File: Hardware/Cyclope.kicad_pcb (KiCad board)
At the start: 2 copper layers, 100 x 84 mm, 81 parts, among them J1 M20-9762042, J2 Motor_2, J3 Motor_1, J4 Front, J5 Front, J8 FTDI, M1 FS5113R, M2 FS5113R, Q1 DMG3414U, Q2 DMG2301L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

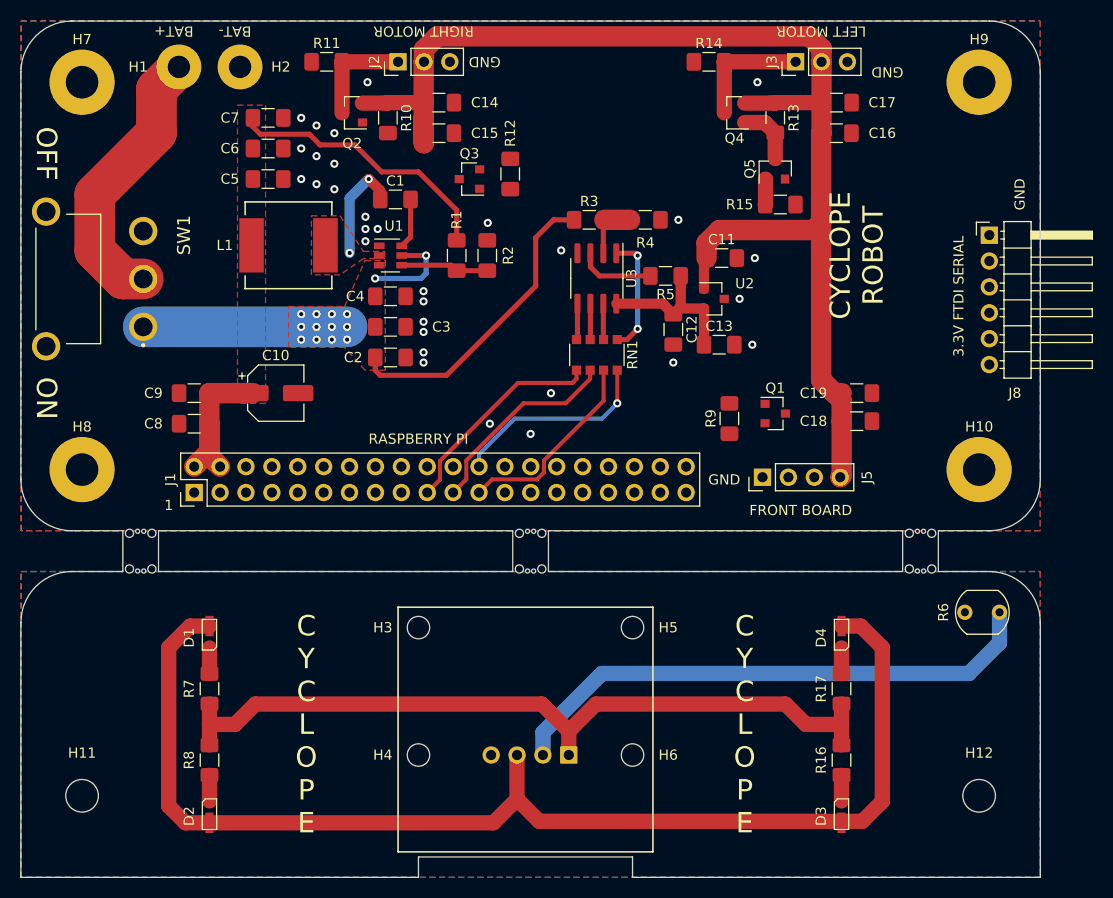
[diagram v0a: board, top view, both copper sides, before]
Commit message: [Hardware] Added larger tracks and a return path for motherboard PCB +5V.
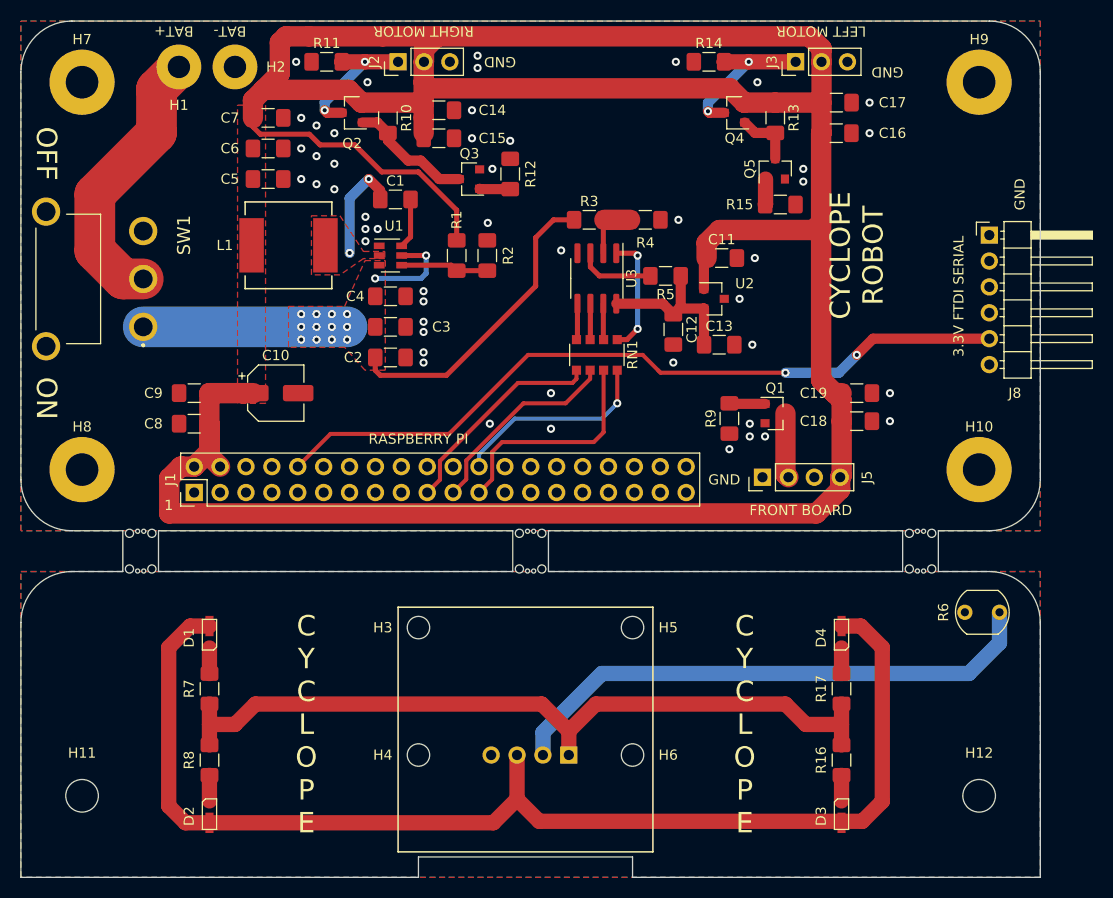
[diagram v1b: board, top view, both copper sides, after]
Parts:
- moved C14 0.75 mm to (98.5, 68.8)
- moved C15 0.50 mm to (98.5, 71.5)
- moved H2 0.50 mm to (78.5, 64.5)
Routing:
- net +5V: track 171.7 -> 317.3 mm
- net /Raspberry_Pi/UART_RX: track 0.00 -> 74.5 mm, vias 0 -> 2
- net Net-(Q2-Pad1): track 0.00 -> 12.2 mm
- net Net-(J5-Pad2): track 0.00 -> 6.37 mm
- net FRONT_BOARD_LEDS: track 0.00 -> 3.52 mm
- net Net-(J2-Pad1): track 10.5 -> 13.7 mm, vias 0 -> 2
- net Net-(J3-Pad1): track 12.0 -> 15.2 mm, vias 0 -> 2
- net Net-(J1-Pad33): track 0.00 -> 3.02 mm
- net ADC_SPI_SCK: track 19.6 -> 22.3 mm
- net GND: vias 31 -> 49

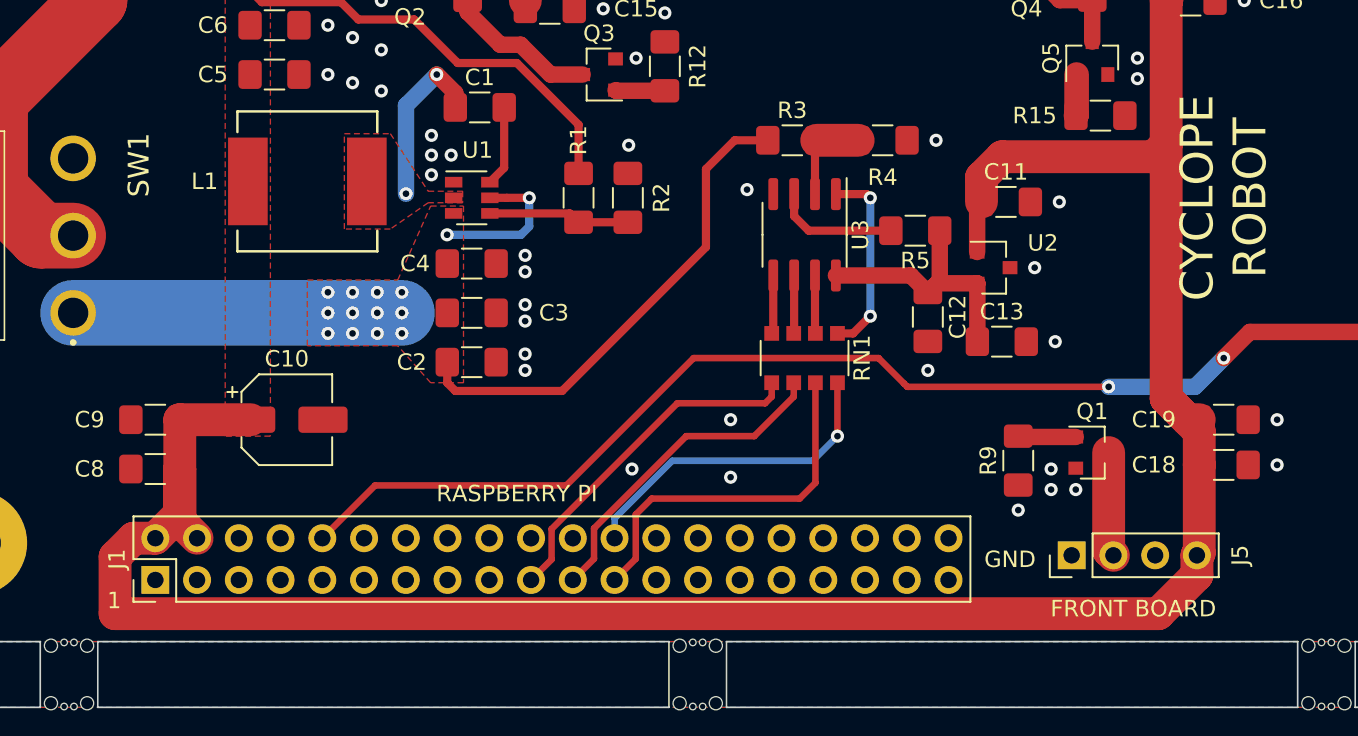
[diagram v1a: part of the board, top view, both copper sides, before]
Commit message: [Hardware] Changed some motherboard connectors connection type with ground planes to decrease impedance.
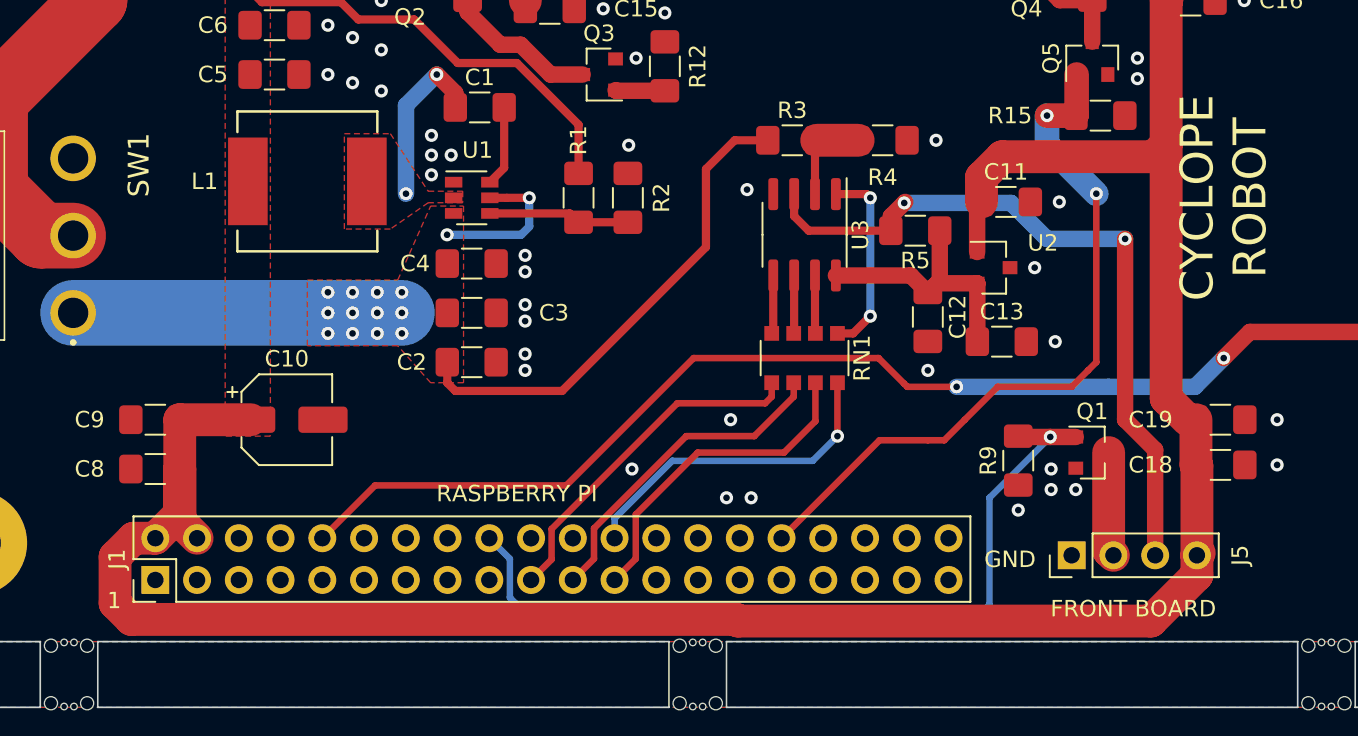
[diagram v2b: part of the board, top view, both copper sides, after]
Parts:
- moved C18 0.20 mm to (139.3, 99.2)
- moved C19 0.20 mm to (139.3, 96.5)
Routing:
- net FRONT_BOARD_LEDS: track 3.52 -> 49.2 mm, vias 0 -> 1
- net Net-(J1-Pad32): track 2.52 -> 44.1 mm, vias 0 -> 2
- net FRONT_BOARD_LDR: track 7.59 -> 44.1 mm, vias 0 -> 2
- net +5V: track 317.3 -> 314.6 mm
- net ADC_SPI_SCK: track 22.3 -> 20.1 mm
- net GND: vias 49 -> 50

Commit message: [Hardware] Improved component names placement on motherboard PCB.
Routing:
- net /Raspberry_Pi/UART_TX: track 0.00 -> 87.5 mm
- net Net-(J1-Pad33): track 3.02 -> 40.1 mm, vias 0 -> 1
- net GND: vias 50 -> 52
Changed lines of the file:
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@@
     (thickness 1.6)
     (drawings 66)
-    (tracks 355)
+    (tracks 376)
     (zones 0)
     (modules 81)
@@
   )
   (setup
-    (last_trace_width 2)
+    (last_trace_width 0.4)
     (user_trace_width 0.4)
     (user_trace_width 0.5)
@@
     (tags "capacitor handsolder")
     (attr smd)
-    (fp_text reference C12 (at 0 -1.82 90) (layer F.SilkS)
+    (fp_text reference C12 (at 0 2 90) (layer F.SilkS)
       (effects (font (size 1 1) (thickness 0.15)))
     )
@@
     (tags "mounting hole 2.2mm m2")
     (attr virtual)
-    (fp_text reference H1 (at 0 3.75) (layer F.SilkS)
+    (fp_text reference H1 (at -3.75 0) (layer F.SilkS)
       (effects (font (size 1 1) (thickness 0.15)))
     )
@@
     (tags "capacitor handsolder")
     (attr smd)
-    (fp_text reference C4 (at 3.45 0) (layer F.SilkS)
+    (fp_text reference C4 (at -4.75 0) (layer F.SilkS)
       (effects (font (size 1 1) (thickness 0.15)))
     )
@@
     (tags "capacitor handsolder")
     (attr smd)
-    (fp_text reference C3 (at -5 0) (layer F.SilkS)
+    (fp_text reference C3 (at -4.75 0) (layer F.SilkS)
       (effects (font (size 1 1) (thickness 0.15)))
     )
@@
     (tags "capacitor handsolder")
     (attr smd)
-    (fp_text reference C2 (at 3.65 0) (layer F.SilkS)
+    (fp_text reference C2 (at -4.75 0) (layer F.SilkS)
       (effects (font (size 1 1) (thickness 0.15)))
     )
@@
     (effects (font (size 1 1) (thickness 0.15)))
   )
-  (gr_text GND (at 142.5 65 180) (layer F.SilkS)
+  (gr_text GND (at 143.5 64 180) (layer F.SilkS)
     (effects (font (size 1 1) (thickness 0.15)))
   )
@@
   (via (at 101.75 68.75) (size 0.8) (drill 0.4) (layers F.Cu B.Cu) (net 3))
   (via (at 84.5 64) (size 0.8) (drill 0.4) (layers F.Cu B.Cu) (net 3))
-  (via (at 102.3 63.4) (size 0.8) (drill 0.4) (layers F.Cu B.Cu) (net 3))
-  (via (at 102.3 64.6) (size 0.8) (drill 0.4) (layers F.Cu B.Cu) (net 3))
+  (via (at 102.3 63.5) (size 0.8) (drill 0.4) (layers F.Cu B.Cu) (net 3))
+  (via (at 102.3 64.75) (size 0.8) (drill 0.4) (layers F.Cu B.Cu) (net 3))
   (via (at 109.25 101.25) (size 0.8) (drill 0.4) (layers F.Cu B.Cu) (net 3))
   (via (at 110.75 101.25) (size 0.8) (drill 0.4) (layers F.Cu B.Cu) (net 3))
+  (via (at 141.25 63.5) (size 0.8) (drill 0.4) (layers F.Cu B.Cu) (net 3))
+  (via (at 141.25 64.75) (size 0.8) (drill 0.4) (layers F.Cu B.Cu) (net 3))
   (segment (start 136.04 70.96) (end 136 71) (width 2) (layer F.Cu) (net 4))
   (segment (start 136.04 64) (end 136.04 70.96) (width 2) (layer F.Cu) (net 4))
@@
   (segment (start 102.5375 76.4875) (end 102.5 76.45) (width 1) (layer F.Cu) (net 12))
   (segment (start 105.5 76.4875) (end 102.5375 76.4875) (width 1) (layer F.Cu) (net 12))
+  (segment (start 116.429999 104.960001) (end 116.429999 100.870001) (width 0.4) (layer B.Cu) (net 12))
+  (segment (start 115.14 106.25) (end 116.429999 104.960001) (width 0.4) (layer B.Cu) (net 12))
+  (segment (start 116.429999 100.870001) (end 119.1 98.2) (width 0.4) (layer B.Cu) (net 12))
+  (segment (start 119.1 98.2) (end 119.1 96.2) (width 0.4) (layer B.Cu) (net 12))
+  (segment (start 119.1 96.2) (end 106.9 84) (width 0.4) (layer B.Cu) (net 12))
+  (segment (start 106.9 84) (end 106.9 80.2) (width 0.4) (layer B.Cu) (net 12))
+  (segment (start 106.9 80.2) (end 106.7 80) (width 0.4) (layer B.Cu) (net 12))
+  (segment (start 106.7 80) (end 106.7 80) (width 0.4) (layer B.Cu) (net 12))
+  (via (at 106.7 80) (size 0.8) (drill 0.4) (layers F.Cu B.Cu) (net 12))
+  (segment (start 106.7 77.6875) (end 105.5 76.4875) (width 1) (layer F.Cu) (net 12))
+  (segment (start 106.7 80) (end 106.7 77.6875) (width 1) (layer F.Cu) (net 12))
   (segment (start 130.55 77.9625) (end 130.5125 78) (width 1.5) (layer F.Cu) (net 13))
   (segment (start 130.55 75.5) (end 130.55 77.9625) (width 1.5) (layer F.Cu) (net 13))
@@
   (via (at 123.25 94.5) (size 0.8) (drill 0.4) (layers F.Cu B.Cu) (net 46))
   (segment (start 132.5 94.5) (end 123.25 94.5) (width 1) (layer B.Cu) (net 46))
+  (segment (start 147.1 90) (end 148.48 88.62) (width 0.4) (layer B.Cu) (net 47))
+  (segment (start 147.1 99.2) (end 147.1 90) (width 0.4) (layer B.Cu) (net 47))
+  (segment (start 85.15001 108.85001) (end 137.44999 108.85001) (width 0.4) (layer B.Cu) (net 47))
+  (segment (start 137.44999 108.85001) (end 147.1 99.2) (width 0.4) (layer B.Cu) (net 47))
+  (segment (start 83.409999 107.109999) (end 85.15001 108.85001) (width 0.4) (layer B.Cu) (net 47))
+  (segment (start 83.409999 104.999999) (end 83.409999 107.109999) (width 0.4) (layer B.Cu) (net 47))
+  (segment (start 148.48 88.62) (end 152.5 88.62) (width 0.4) (layer B.Cu) (net 47))
+  (segment (start 82.12 103.71) (end 83.409999 104.999999) (width 0.4) (layer B.Cu) (net 47))
   (segment (start 88.9875 64) (end 91.25 64) (width 1.5) (layer F.Cu) (net 51))
   (segment (start 89 64.0125) (end 88.9875 64) (width 1.5) (layer F.Cu) (net 51))

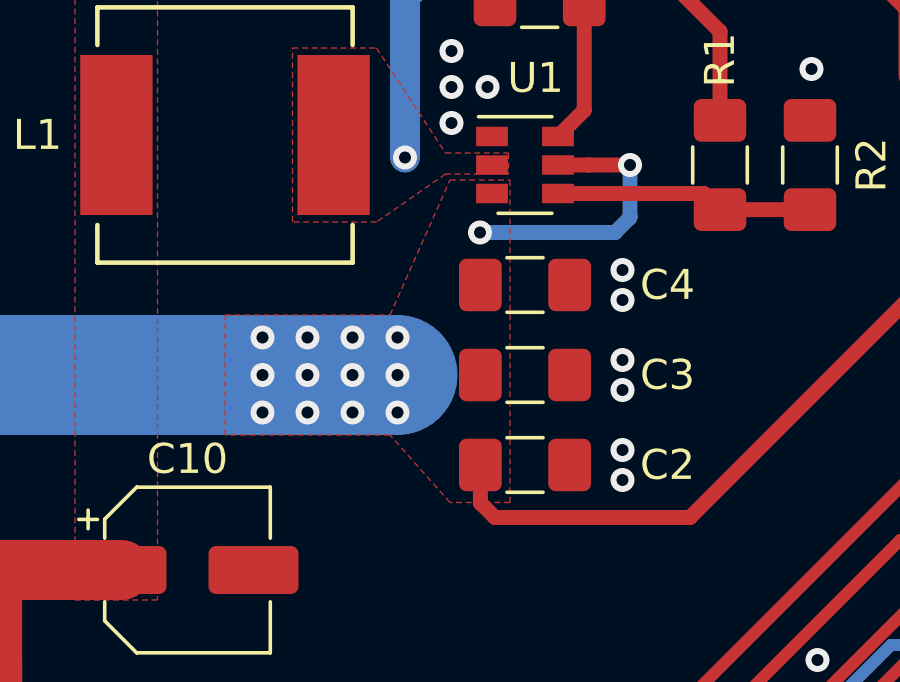
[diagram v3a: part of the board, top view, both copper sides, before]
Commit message: [Hardware] Let more space between TPS565208 'Vin' and 'SW' copper areas.
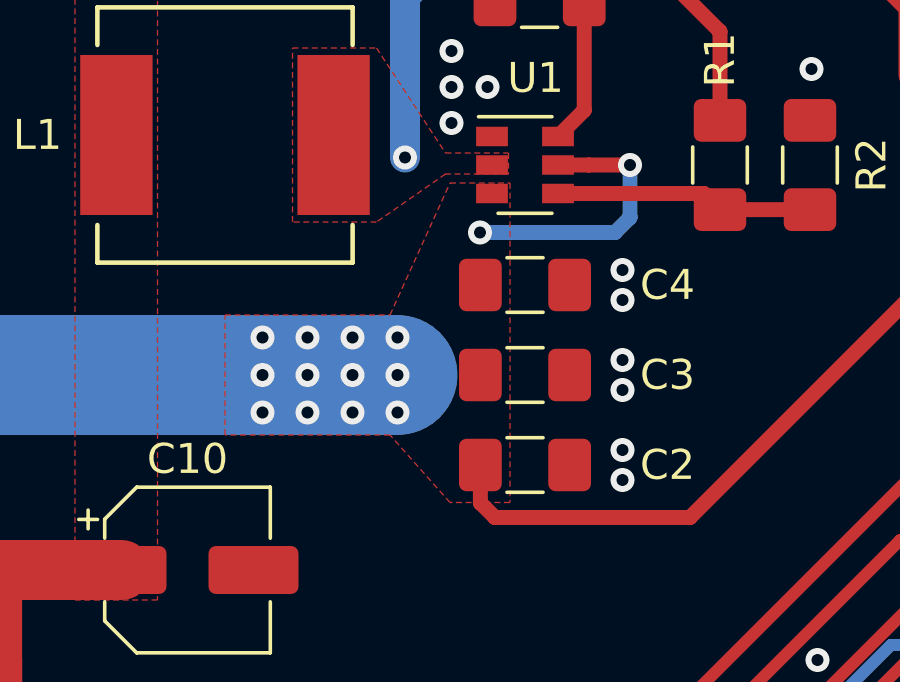
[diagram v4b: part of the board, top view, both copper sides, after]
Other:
- net class Default: clearance 0.2 -> 0.25
- rule trace_clearance: 0.2 -> 0.25
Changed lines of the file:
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@@
     (user_trace_width 3)
     (user_trace_width 4)
-    (trace_clearance 0.2)
+    (trace_clearance 0.25)
     (zone_clearance 0.127)
     (zone_45_only no)
@@
   (net 61 "Net-(SW1-Pad3)")
   (net_class Default "Ceci est la Netclass par défaut."
-    (clearance 0.2)
+    (clearance 0.25)
     (trace_width 0.25)
     (via_dia 0.8)
@@
       (pts
         (xy 93.25 94.25) (xy 91.25 94.25) (xy 89.25 92) (xy 83.75 92) (xy 83.75 88)
-        (xy 89.25 88) (xy 91.25 83.5) (xy 93.25 83.5)
+        (xy 89.25 88) (xy 91.25 83.6) (xy 93.25 83.6)
       )
     )
